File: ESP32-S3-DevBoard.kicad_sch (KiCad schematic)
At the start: 27 parts, among them J1 USB_C_Receptacle_USB2.0_14P, J2 Conn_01x22_Socket, J3 Conn_01x22_Socket, SW1 SW_Push, SW2 SW_Push, U1 ESP32-S3-WROOM-1, U2 AMS1117-3.3

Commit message: Update USB-C footprint
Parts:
- J1: footprint Connector_USB:USB_C_Receptacle_GCT_USB4125-xx-x_6P_TopMnt_Horizontal -> Connector_USB:USB_C_Receptacle_GCT_USB4105-xx-A_16P_TopMnt_Horizontal
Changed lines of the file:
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@@
 			)
 		)
-		(property "Footprint" "Connector_USB:USB_C_Receptacle_GCT_USB4125-xx-x_6P_TopMnt_Horizontal"
+		(property "Footprint" "Connector_USB:USB_C_Receptacle_GCT_USB4105-xx-A_16P_TopMnt_Horizontal"
 			(at 111.76 140.97 0)
 			(effects

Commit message: Finish layout
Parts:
- D3, D4, D5: footprint Diode_SMD:D_SOD-323 -> Diode_SMD:D_SOD-323_HandSoldering
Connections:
- net GND: now also J3.1 (Pin_1)
- net VCC_5V: no longer J3.1 (Pin_1)
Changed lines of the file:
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@@
 			)
 		)
-		(property "Footprint" "Diode_SMD:D_SOD-323"
+		(property "Footprint" "Diode_SMD:D_SOD-323_HandSoldering"
 			(at 130.81 158.75 0)
 			(effects
@@
 			)
 		)
-		(property "Footprint" "Diode_SMD:D_SOD-323"
+		(property "Footprint" "Diode_SMD:D_SOD-323_HandSoldering"
 			(at 156.21 158.75 0)
 			(effects
@@
 			)
 		)
-		(property "Footprint" "Diode_SMD:D_SOD-323"
+		(property "Footprint" "Diode_SMD:D_SOD-323_HandSoldering"
 			(at 124.46 158.75 0)
 			(effects
@@
 	)
 	(symbol
-		(lib_id "power:+5V")
-		(at 66.04 118.11 0)
-		(unit 1)
-		(exclude_from_sim no)
-		(in_bom yes)
-		(on_board yes)
-		(dnp no)
-		(property "Reference" "#PWR019"
-			(at 66.04 121.92 0)
-			(effects
-				(font
-					(size 1.27 1.27)
-				)
-				(hide yes)
-			)
-		)
-		(property "Value" "VCC_5V"
-			(at 66.04 113.03 0)
-			(effects
-				(font
-					(size 1.27 1.27)
-				)
-			)
-		)
-		(property "Footprint" ""
-			(at 66.04 118.11 0)
-			(effects
-				(font
-					(size 1.27 1.27)
-				)
-				(hide yes)
-			)
-		)
-		(property "Datasheet" ""
-			(at 66.04 118.11 0)
-			(effects
-				(font
-					(size 1.27 1.27)
-				)
-				(hide yes)
-			)
-		)
-		(property "Description" "Power symbol creates a global label with name \"+5V\""
-			(at 66.04 118.11 0)
-			(effects
-				(font
-					(size 1.27 1.27)
-				)
-				(hide yes)
-			)
-		)
-		(pin "1"
-		)
-		(instances
-			(project "ESP32-S3-DevBoard"
-				(path "/b53eb8a5-cc6c-490f-9a0c-2a07c0a6a3dd"
-					(reference "#PWR019")
-					(unit 1)
-				)
-			)
-		)
-	)
-	(symbol
 		(lib_id "power:+3.3V")
 		(at 31.75 30.48 0)
@@
 					(unit 1)
 				)
+			)
+		)
+	)
+	(symbol
+		(lib_id "power:GND")
+		(at 66.04 118.11 180)
+		(unit 1)
+		(exclude_from_sim no)
+		(in_bom yes)
+		(on_board yes)
+		(dnp no)
+		(fields_autoplaced yes)
+		(property "Reference" "#PWR019"
+			(at 66.04 111.76 0)
+			(effects
+				(font
+					(size 1.27 1.27)
+				)
+				(hide yes)
+			)
+		)
+		(property "Value" "GND"
+			(at 66.04 113.03 0)
+			(effects
+				(font
+					(size 1.27 1.27)
+				)
+			)
+		)
+		(property "Footprint" ""
+			(at 66.04 118.11 0)
+			(effects
+				(font
+					(size 1.27 1.27)
+				)
+				(hide yes)
+			)
+		)
+		(property "Datasheet" ""
+			(at 66.04 118.11 0)
+			(effects
+				(font
+					(size 1.27 1.27)
+				)
+				(hide yes)
+			)
+		)
+		(property "Description" "Power symbol creates a global label with name \"GND\" , ground"
+			(at 66.04 118.11 0)
+			(effects
+				(font
+					(size 1.27 1.27)
+				)
+				(hide yes)
+			)
+		)
+		(pin "1"
+		)
+		(instances
+			(project "ESP32-S3-DevBoard"
+				(path "/b53eb8a5-cc6c-490f-9a0c-2a07c0a6a3dd"
+					(reference "#PWR019")
+					(unit 1)
+				)

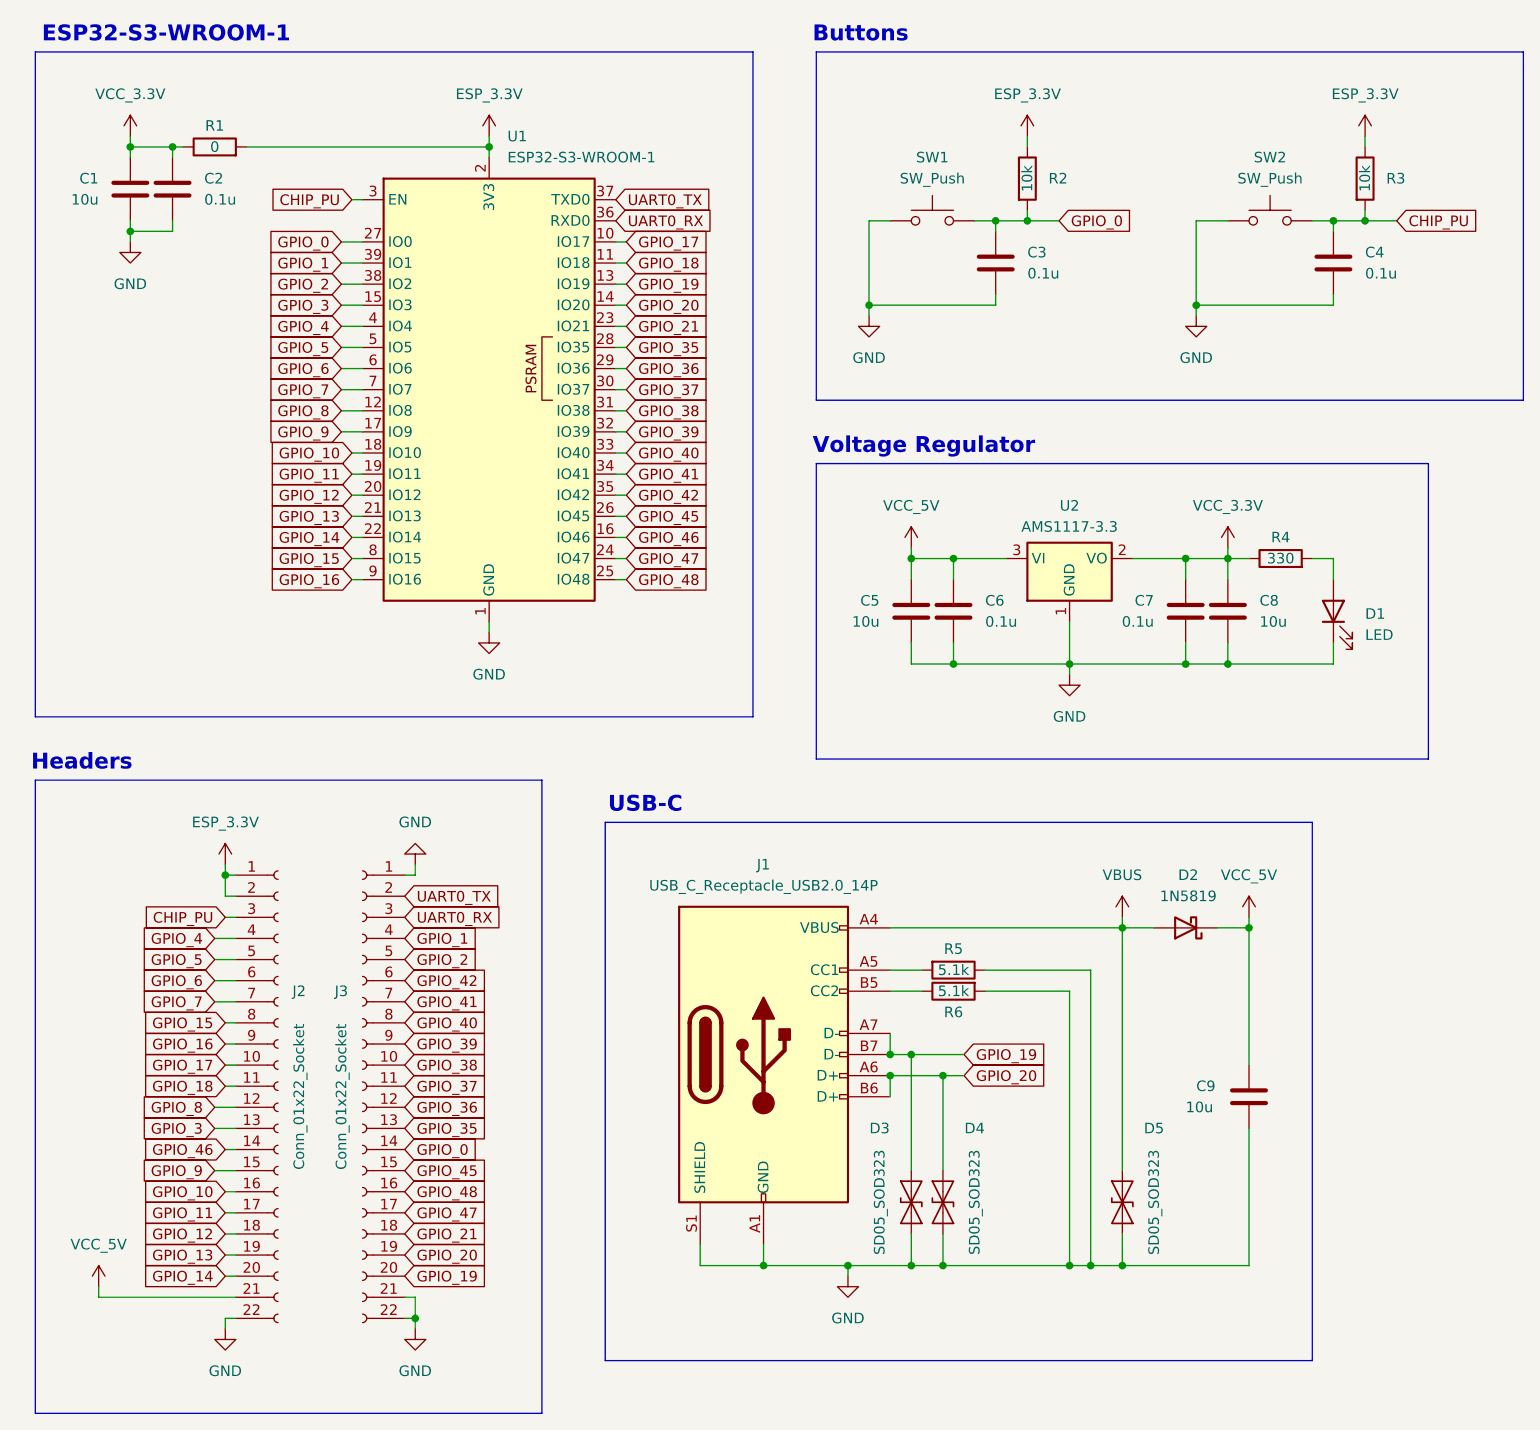
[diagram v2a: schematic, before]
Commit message: Add impedance matching for USB lines
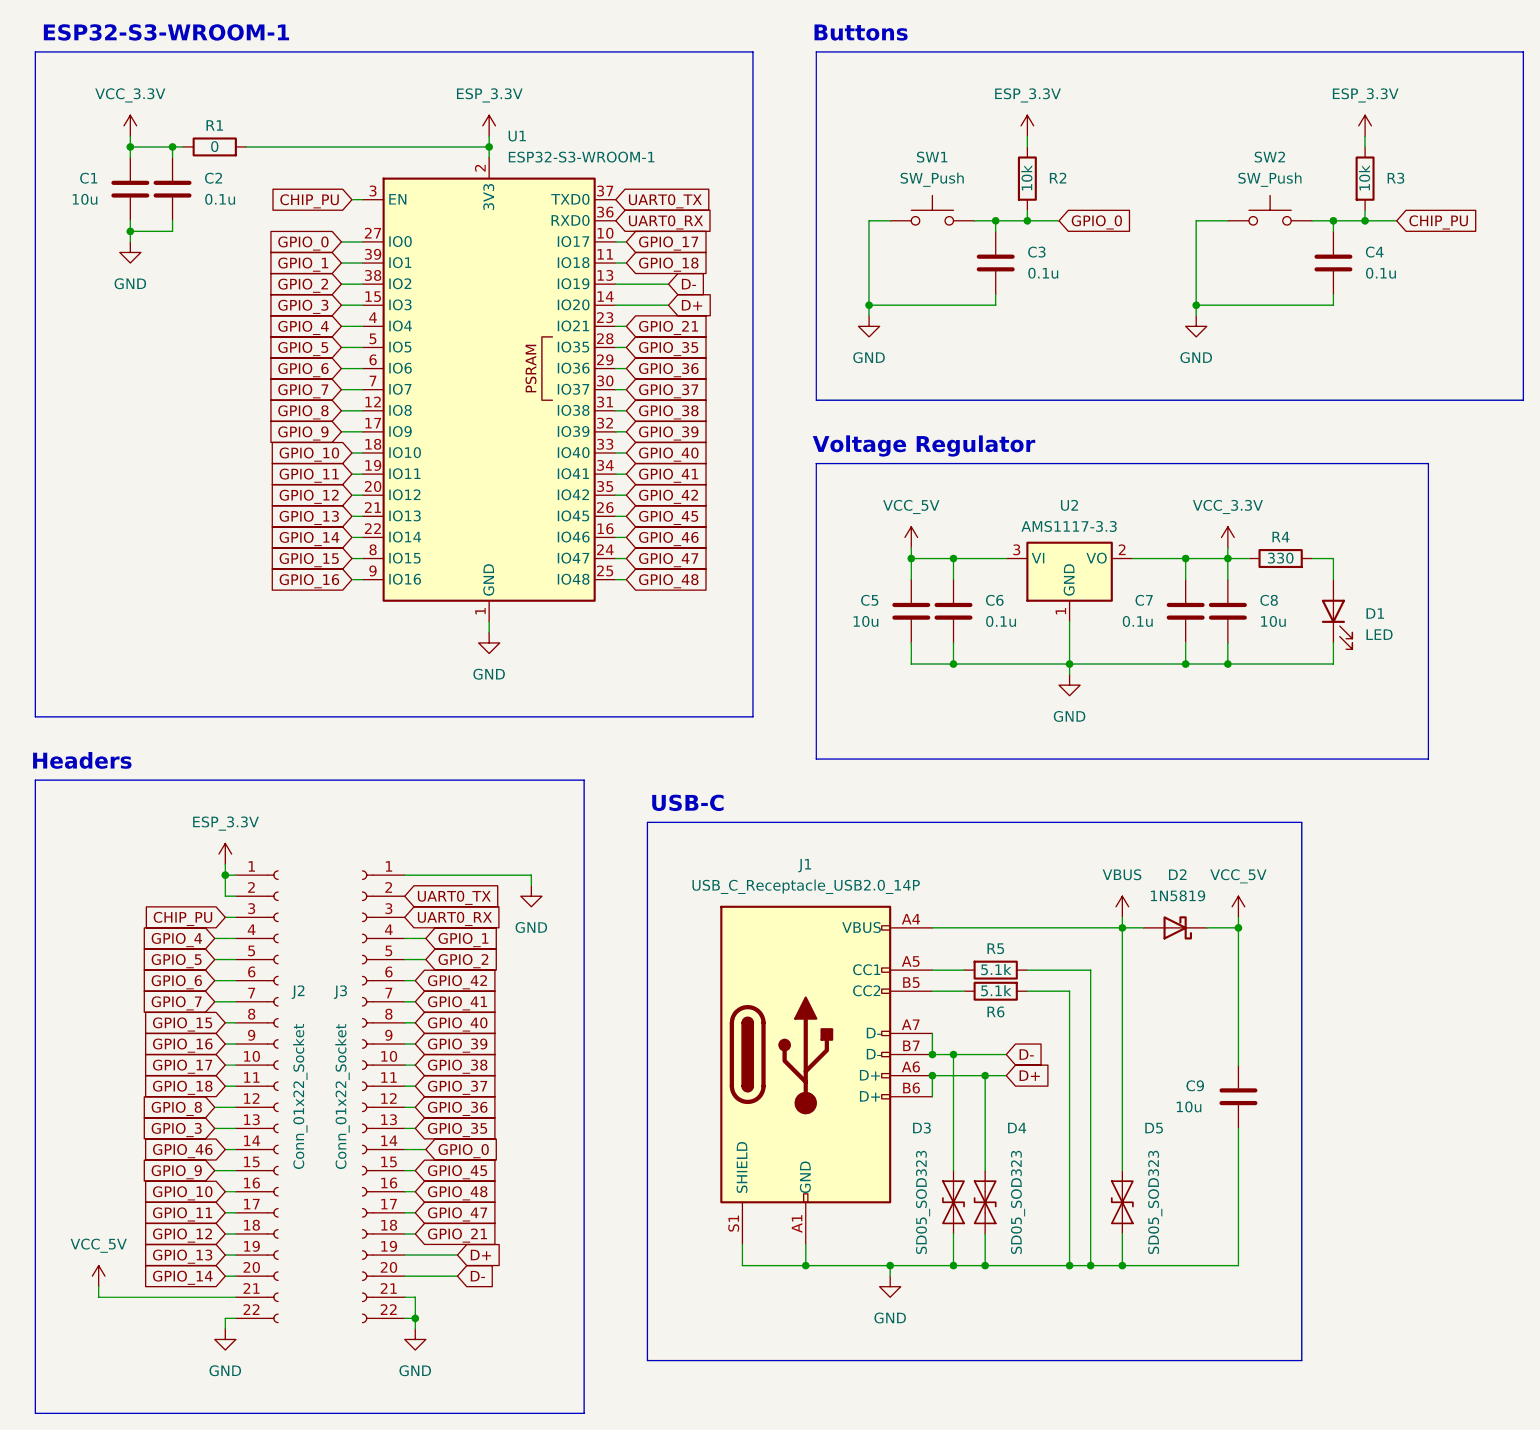
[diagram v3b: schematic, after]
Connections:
- net GPIO_19 renamed D-
- net GPIO_20 renamed D+
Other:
- moved on the sheet: C9, D2, D3, D4, J1, R5, R6
